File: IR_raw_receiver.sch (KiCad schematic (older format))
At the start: 5 parts

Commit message: Might be done already :-)
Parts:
- added C1: 47µF, symbol CP1
- added MH1, MH2, MH3, MH4: CONN_1, symbol CONN_1
- added P1: CONN_5, symbol CONN_5
- added R2, R3, R4, R5: 1k, symbol R
- JP1: renamed from JP?; value MADW__AVR_ISP -> ISP
- Q1: renamed from Q?; value CSTLA_T -> 8MHz
- R1: renamed from R?; value R -> 10k
- U1: renamed from U?; value MADW__TSOP38238 -> TSOP38238
- gave numbers to parts that had none: 1
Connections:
- net labels added: GND, MISO, MOSI, RESET, SCK, VCC, XTAL1, XTAL2
- wire segments 0 -> 38
- no-connect marks 0 -> 4
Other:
- moved on the sheet: IC1, JP1, Q1, R1, U1

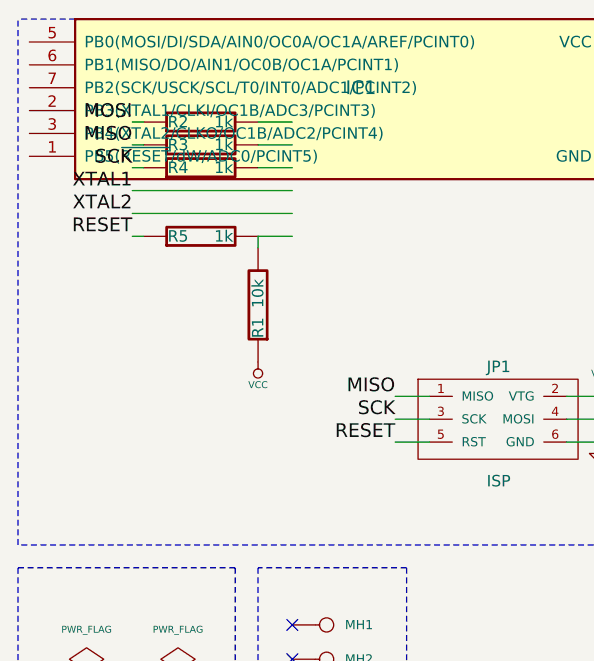
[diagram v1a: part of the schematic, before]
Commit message: Added a LED + some minor tweaks.
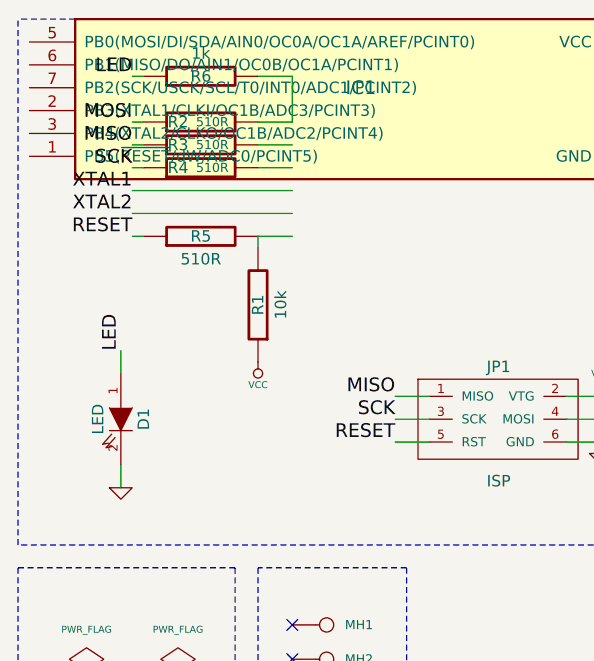
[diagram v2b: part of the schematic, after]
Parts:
- added D1: LED, symbol LED
- added R6: 1k, symbol R
- R2, R3, R4, R5: value 1k -> 510R
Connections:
- net labels added: LED
- wire segments 38 -> 43
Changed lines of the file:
@@
-EESchema Schematic File Version 2  date Sun 25 Mar 2012 02:18:25 PM CEST
+EESchema Schematic File Version 2  date Sun 25 Mar 2012 06:06:28 PM CEST
 LIBS:power
 LIBS:device
@@
 Comment4 ""
 $EndDescr
+Text Label 1650 2700 1    60   ~ 0
+LED
+Wire Wire Line
+	1650 2800 1650 2700
+Wire Wire Line
+	1750 1500 1700 1500
+Wire Notes Line
+	2900 3650 2250 3650
+Wire Notes Line
+	2900 3650 2900 4600
+Wire Notes Line
+	2900 4600 2250 4600
+Wire Notes Line
+	2250 4600 2250 3650
+Wire Notes Line
+	5650 1250 1200 1250
+Wire Notes Line
+	5650 1250 5650 3550
+Wire Notes Line
+	5650 3550 1200 3550
+Wire Notes Line
+	1200 3550 1200 1250
+Connection ~ 5200 2200
+Wire Wire Line
+	5200 2150 5200 2250
+Wire Wire Line
+	6850 1900 6950 1900
+Wire Wire Line
+	1700 1700 1750 1700
+Wire Wire Line
+	1700 1900 1750 1900
+Wire Wire Line
+	1700 2100 2400 2100
+Wire Wire Line
+	6250 3150 6350 3150
+Wire Wire Line
+	1900 4150 1900 4250
+Wire Wire Line
+	6950 2300 6950 2250
+Wire Wire Line
+	6950 2250 6850 2250
+Wire Wire Line
+	5200 2200 5100 2200
+Wire Wire Line
+	2250 1700 2400 1700
+Wire Wire Line
+	2250 1900 2400 1900
+Wire Wire Line
+	4800 2900 4850 2900
+Wire Wire Line
+	4600 3200 4600 3300
+Wire Wire Line
+	3600 3000 3750 3000
+Wire Wire Line
+	3000 3100 2850 3100
+Wire Wire Line
+	3000 2900 2850 2900
+Wire Wire Line
+	2250 2250 2250 2200
+Wire Wire Line
+	2250 2200 2400 2200
+Wire Wire Line
+	3000 3000 2850 3000
+Wire Wire Line
+	3600 2900 3750 2900
+Wire Wire Line
+	3600 3100 3750 3100
+Wire Wire Line
+	4400 2900 4350 2900
+Wire Wire Line
+	3750 3100 3750 3150
+Wire Wire Line
+	2250 1800 2400 1800
+Wire Wire Line
+	5100 1700 5200 1700
+Wire Wire Line
+	6850 1550 6950 1550
+Wire Wire Line
+	6950 1550 6950 1500
+Wire Wire Line
+	1500 4150 1500 4250
+Wire Wire Line
+	6350 2850 6250 2850
+Wire Wire Line
+	6250 3050 6350 3050
+Wire Wire Line
+	6350 3250 6250 3250
+Wire Wire Line
+	2400 2000 1700 2000
+Wire Wire Line
+	1750 1800 1700 1800
+Wire Wire Line
+	1700 2200 1750 2200
+Wire Wire Line
+	6150 2900 6150 2950
+Wire Wire Line
+	6150 2950 6350 2950
+Wire Wire Line
+	5200 1700 5200 1750
+Wire Notes Line
+	1200 4600 1200 3650
+Wire Notes Line
+	1200 4600 2150 4600
+Wire Notes Line
+	1200 3650 2150 3650
+Wire Notes Line
+	5800 3550 5800 1250
+Wire Notes Line
+	5800 3550 7350 3550
+Wire Notes Line
+	7350 3550 7350 1250
+Wire Notes Line
+	7350 1250 5800 1250
+Wire Notes Line
+	2150 3650 2150 4600
+Wire Wire Line
+	2250 1500 2400 1500
+Wire Wire Line
+	2400 1500 2400 1700
+Wire Wire Line
+	1650 3200 1650 3300
+$Comp
+L GND #PWR01
+U 1 1 4F6F3657
+P 1650 3300
+F 0 "#PWR01" H 1650 3300 30  0001 C CNN
+F 1 "GND" H 1650 3230 30  0001 C CNN
+	1    1650 3300
+	1    0    0    -1
+$EndComp
+Text Label 1700 1500 2    60   ~ 0
+LED
+$Comp
+L LED D1
+U 1 1 4F6F3628
+P 1650 3000
+F 0 "D1" H 1650 3100 50  0000 C CNN
+F 1 "LED" H 1650 2900 50  0000 C CNN
+	1    1650 3000
+	0    1    1    0
+$EndComp
+$Comp
+L R R6
+U 1 1 4F6F35F5
+P 2000 1500
+F 0 "R6" V 2000 1500 50  0000 C CNN
+F 1 "1k" V 2100 1500 50  0000 C CNN
+	1    2000 1500
+	0    -1   -1   0
+$EndComp
 NoConn ~ 2400 4350
 NoConn ~ 2400 4200
 NoConn ~ 2400 4050
 NoConn ~ 2400 3900
-Wire Notes Line
-	2900 3650 2250 3650
-Wire Notes Line
-	2900 3650 2900 4600
-Wire Notes Line
-	2900 4600 2250 4600
-Wire Notes Line
-	2250 4600 2250 3650
-Wire Notes Line
-	5650 1250 1200 1250
-Wire Notes Line
-	5650 1250 5650 3550
-Wire Notes Line
-	5650 3550 1200 3550
-Wire Notes Line
-	1200 3550 1200 1250
-Connection ~ 5200 2200
-Wire Wire Line
-	5200 2150 5200 2250
-Wire Wire Line
-	6850 1900 6950 1900
-Wire Wire Line
-	1700 1700 1750 1700
-Wire Wire Line
-	1700 1900 1750 1900
-Wire Wire Line
-	1700 2100 2400 2100
-Wire Wire Line
-	6250 3150 6350 3150
-Wire Wire Line
-	1900 4150 1900 4250
-Wire Wire Line
-	6950 2300 6950 2250
-Wire Wire Line
-	6950 2250 6850 2250
-Wire Wire Line
-	5200 2200 5100 2200
-Wire Wire Line
-	2250 1700 2400 1700
-Wire Wire Line
-	2250 1900 2400 1900
-Wire Wire Line
-	4800 2900 4850 2900
-Wire Wire Line
-	4600 3200 4600 3300
-Wire Wire Line
-	3600 3000 3750 3000
-Wire Wire Line
-	3000 3100 2850 3100
-Wire Wire Line
-	3000 2900 2850 2900
-Wire Wire Line
-	2250 2250 2250 2200
-Wire Wire Line
-	2250 2200 2400 2200
-Wire Wire Line
-	3000 3000 2850 3000
-Wire Wire Line
-	3600 2900 3750 2900
-Wire Wire Line
-	3600 3100 3750 3100
-Wire Wire Line
-	4400 2900 4350 2900
-Wire Wire Line
-	3750 3100 3750 3150
-Wire Wire Line
-	2250 1800 2400 1800
-Wire Wire Line
-	5100 1700 5200 1700
-Wire Wire Line
-	6850 1550 6950 1550
-Wire Wire Line
-	6950 1550 6950 1500
-Wire Wire Line
-	1500 4150 1500 4250
-Wire Wire Line
-	6350 2850 6250 2850
-Wire Wire Line
-	6250 3050 6350 3050
-Wire Wire Line
-	6350 3250 6250 3250
-Wire Wire Line
-	2400 2000 1700 2000
-Wire Wire Line
-	1750 1800 1700 1800
-Wire Wire Line
-	1700 2200 1750 2200
-Wire Wire Line
-	6150 2900 6150 2950
-Wire Wire Line
-	6150 2950 6350 2950
-Wire Wire Line
-	5200 1700 5200 1750
-Wire Notes Line
-	1200 4600 1200 3650
-Wire Notes Line
-	1200 4600 2150 4600
-Wire Notes Line
-	1200 3650 2150 3650
-Wire Notes Line
-	5800 3550 5800 1250
-Wire Notes Line
-	5800 3550 7350 3550
-Wire Notes Line
-	7350 3550 7350 1250
-Wire Notes Line
-	7350 1250 5800 1250
-Wire Notes Line
-	2150 3650 2150 4600
 $Comp
 L CONN_1 MH4
@@
 U 1 1 4F6EEBE3
 P 2000 2200
-F 0 "R5" V 2000 2300 50  0000 C CNN
-F 1 "1k" V 2000 2100 50  0000 C CNN
+F 0 "R5" V 2000 2200 50  0000 C CNN
+F 1 "510R" V 1900 2200 50  0000 C CNN
 	1    2000 2200
 	0    -1   -1   0
@@
 P 2000 1900
 F 0 "R4" V 2000 2000 50  0000 C CNN
-F 1 "1k" V 2000 1800 50  0000 C CNN
+F 1 "510R" V 2000 1850 40  0000 C CNN
 	1    2000 1900
 	0    -1   -1   0
@@
 P 2000 1800
 F 0 "R3" V 2000 1900 50  0000 C CNN
-F 1 "1k" V 2000 1700 50  0000 C CNN
+F 1 "510R" V 2000 1750 40  0000 C CNN
 	1    2000 1800
 	0    -1   -1   0
@@
 P 2000 1700
 F 0 "R2" V 2000 1800 50  0000 C CNN
-F 1 "1k" V 2000 1600 50  0000 C CNN
+F 1 "510R" V 2000 1650 40  0000 C CNN
 	1    2000 1700
 	0    -1   -1   0
@@
 MOSI
 $Comp
-L GND #PWR01
+L GND #PWR02
 U 1 1 4F6EEB7B
 P 6150 2900
-F 0 "#PWR01" H 6150 2900 30  0001 C CNN
+F 0 "#PWR02" H 6150 2900 30  0001 C CNN
 F 1 "GND" H 6150 2830 30  0001 C CNN
 	1    6150 2900
@@
 $EndComp
 $Comp
-L VCC #PWR02
+L VCC #PWR03
 U 1 1 4F6EEB71
 P 6250 2850
-F 0 "#PWR02" H 6250 2950 30  0001 C CNN
+F 0 "#PWR03" H 6250 2950 30  0001 C CNN
 F 1 "VCC" H 6250 2950 30  0000 C CNN
 	1    6250 2850
@@
 $EndComp
 $Comp
-L PWR_FLAG #FLG03
+L PWR_FLAG #FLG04
 U 1 1 4F6EE978
 P 1900 4150
-F 0 "#FLG03" H 1900 4420 30  0001 C CNN
+F 0 "#FLG04" H 1900 4420 30  0001 C CNN
 F 1 "PWR_FLAG" H 1900 4380 30  0000 C CNN
 	1    1900 4150
@@
 $EndComp
 $Comp
-L VCC #PWR04
+L VCC #PWR05
 U 1 1 4F6EE956
 P 1900 4250
-F 0 "#PWR04" H 1900 4350 30  0001 C CNN
+F 0 "#PWR05" H 1900 4350 30  0001 C CNN
 F 1 "VCC" H 1900 4350 30  0000 C CNN
 	1    1900 4250
@@
 $EndComp
 $Comp
-L GND #PWR05
+L GND #PWR06
 U 1 1 4F6EE953
 P 1500 4250
-F 0 "#PWR05" H 1500 4250 30  0001 C CNN
+F 0 "#PWR06" H 1500 4250 30  0001 C CNN
 F 1 "GND" H 1500 4180 30  0001 C CNN
 	1    1500 4250
@@
 RESET
 $Comp
-L PWR_FLAG #FLG06
+L PWR_FLAG #FLG07
 U 1 1 4F6EE916
 P 1500 4150
-F 0 "#FLG06" H 1500 4420 30  0001 C CNN
+F 0 "#FLG07" H 1500 4420 30  0001 C CNN
 F 1 "PWR_FLAG" H 1500 4380 30  0000 C CNN
 	1    1500 4150
@@
 $EndComp
 $Comp
-L GND #PWR07
+L GND #PWR08
 U 1 1 4F6EE8F0
 P 6950 2300
-F 0 "#PWR07" H 6950 2300 30  0001 C CNN
+F 0 "#PWR08" H 6950 2300 30  0001 C CNN
 F 1 "GND" H 6950 2230 30  0001 C CNN
 	1    6950 2300
@@
 $EndComp
 $Comp
-L VCC #PWR08
+L VCC #PWR09
 U 1 1 4F6EE8E3
 P 6950 1500
-F 0 "#PWR08" H 6950 1600 30  0001 C CNN
+F 0 "#PWR09" H 6950 1600 30  0001 C CNN
 F 1 "VCC" H 6950 1600 30  0000 C CNN
 	1    6950 1500
@@
 $EndComp
 $Comp
-L VCC #PWR09
+L VCC #PWR010
 U 1 1 4F6EE887
 P 5200 1700
-F 0 "#PWR09" H 5200 1800 30  0001 C CNN
+F 0 "#PWR010" H 5200 1800 30  0001 C CNN
 F 1 "VCC" H 5200 1800 30  0000 C CNN
 	1    5200 1700
@@
 $EndComp
 $Comp
-L GND #PWR010
+L GND #PWR011
 U 1 1 4F6EE882
 P 5200 2250
-F 0 "#PWR010" H 5200 2250 30  0001 C CNN
+F 0 "#PWR011" H 5200 2250 30  0001 C CNN
 F 1 "GND" H 5200 2180 30  0001 C CNN
 	1    5200 2250
@@
 MOSI
 $Comp
-L GND #PWR011
+L GND #PWR012
 U 1 1 4F6EE81E
 P 3750 3150
-F 0 "#PWR011" H 3750 3150 30  0001 C CNN
+F 0 "#PWR012" H 3750 3150 30  0001 C CNN
 F 1 "GND" H 3750 3080 30  0001 C CNN
 	1    3750 3150
@@
 MOSI
 $Comp
-L VCC #PWR012
+L VCC #PWR013
 U 1 1 4F6EE80A
 P 3750 2900
-F 0 "#PWR012" H 3750 3000 30  0001 C CNN
+F 0 "#PWR013" H 3750 3000 30  0001 C CNN
 F 1 "VCC" H 3750 3000 30  0000 C CNN
 	1    3750 2900
@@
 XTAL2
 $Comp
-L GND #PWR013
+L GND #PWR014
 U 1 1 4F6EE7AB
 P 4600 3300
-F 0 "#PWR013" H 4600 3300 30  0001 C CNN
+F 0 "#PWR014" H 4600 3300 30  0001 C CNN
 F 1 "GND" H 4600 3230 30  0001 C CNN
 	1    4600 3300
@@
 $EndComp
 $Comp
-L VCC #PWR014
+L VCC #PWR015
 U 1 1 4F6EE70F
 P 2250 2750
-F 0 "#PWR014" H 2250 2850 30  0001 C CNN
+F 0 "#PWR015" H 2250 2850 30  0001 C CNN
 F 1 "VCC" H 2250 2850 30  0000 C CNN
 	1    2250 2750
@@
 U 1 1 4F6EC6DD
 P 2250 2500
-F 0 "R1" V 2250 2600 50  0000 C CNN
-F 1 "10k" V 2250 2450 50  0000 C CNN
+F 0 "R1" V 2250 2500 50  0000 C CNN
+F 1 "10k" V 2150 2500 50  0000 C CNN
 	1    2250 2500
 	-1   0    0    1

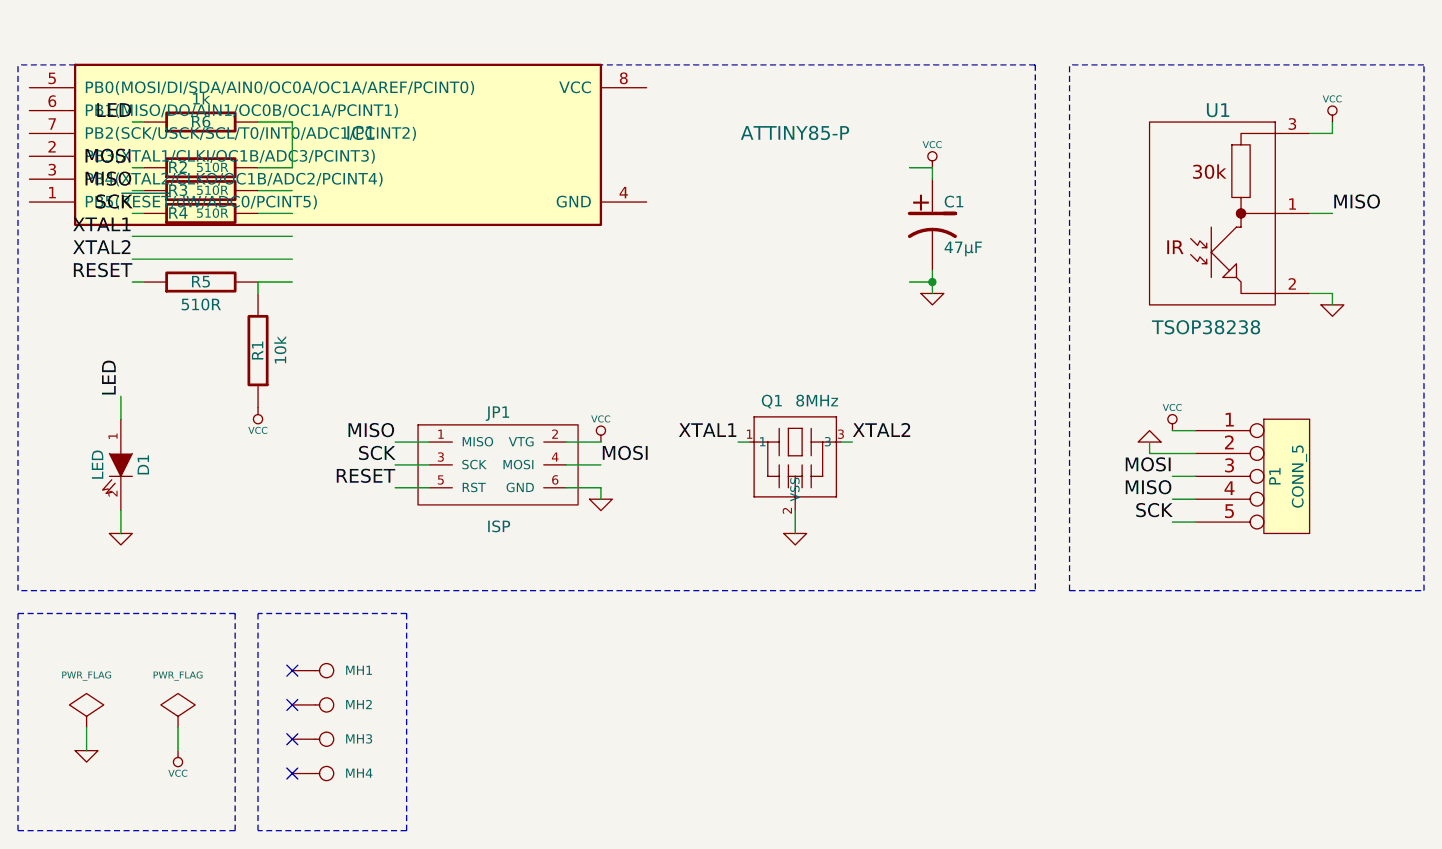
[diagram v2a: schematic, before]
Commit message: Added an L78L05 voltage regulator + caps. Header + silkscreen tweaks.
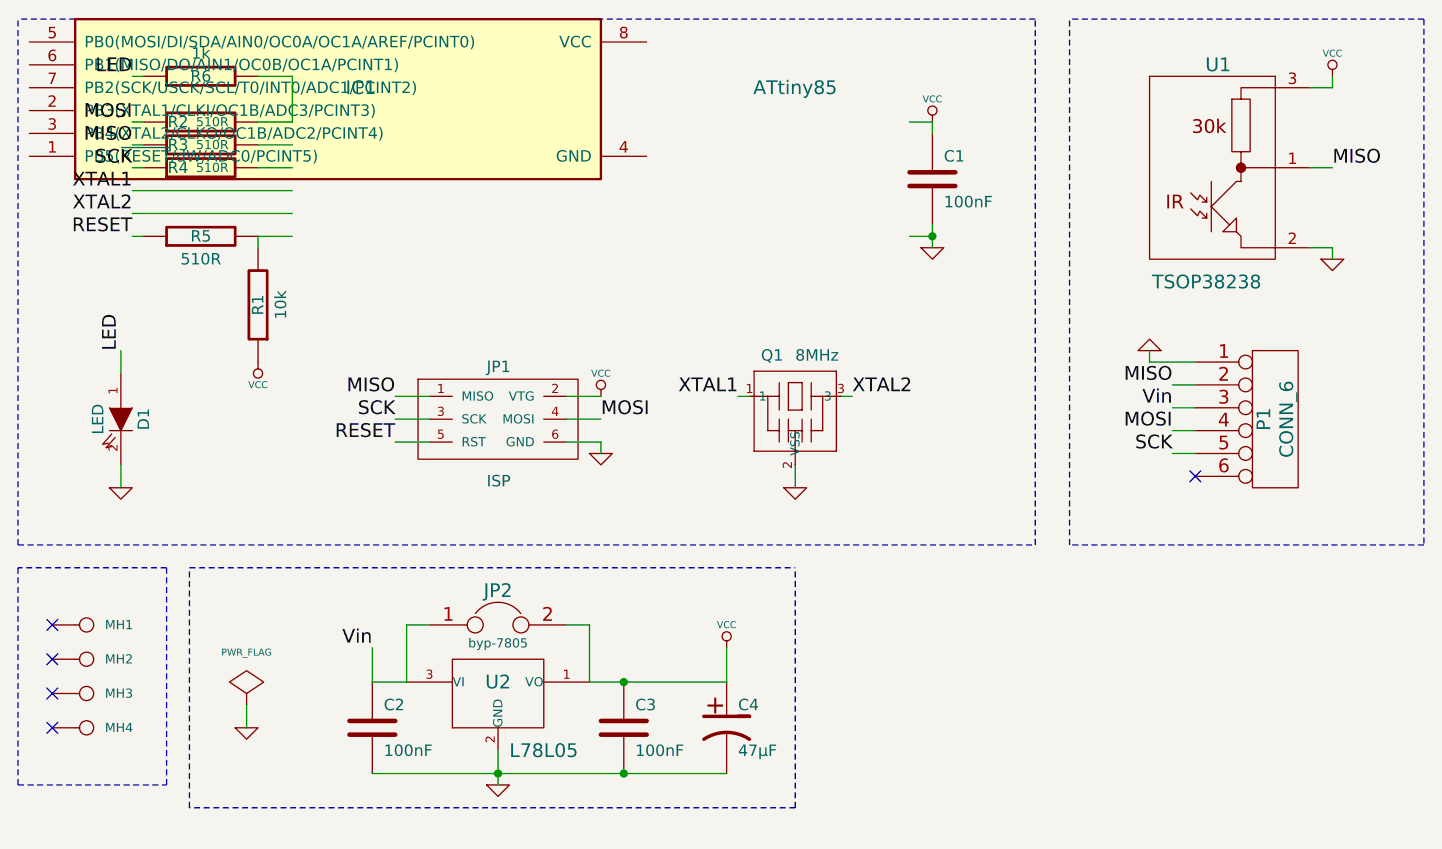
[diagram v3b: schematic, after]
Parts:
- removed P1: CONN_5, symbol CONN_5
- added C1, C2, C3: 100nF, symbol C
- added JP2: byp-7805, symbol JUMPER
- added P1: CONN_6, symbol CONN_6
- added U2: L78L05, symbol MADW__L78L05_TO-92
- IC1: value ATTINY85-P -> ATtiny85
- renumbered C1 to C4
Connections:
- net labels added: Vin
- wire segments 43 -> 52
- no-connect marks 4 -> 5
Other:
- moved on the sheet: C4, D1, IC1, JP1, MH1, MH2, MH3, MH4, Q1, R1, R2, R3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

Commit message: Silkscreen tweaks.
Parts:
- JP2: value byp-7805 -> Vin!
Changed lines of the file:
@@
-EESchema Schematic File Version 2  date Sat 31 Mar 2012 04:20:52 PM CEST
+EESchema Schematic File Version 2  date Sat 31 Mar 2012 09:51:07 PM CEST
 LIBS:power
 LIBS:device
@@
 P 3300 3700
 F 0 "JP2" H 3300 3850 60  0000 C CNN
-F 1 "byp-7805" H 3300 3620 40  0000 C CNN
+F 1 "Vin!" H 3300 3620 40  0000 C CNN
 	1    3300 3700
 	1    0    0    -1

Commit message: Switched to REV. 202 of atmel.lib
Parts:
- IC1: value ATtiny85 -> ATTINY85-P
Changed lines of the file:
@@
-EESchema Schematic File Version 2  date Sat 31 Mar 2012 09:51:07 PM CEST
+EESchema Schematic File Version 2  date Sun 27 Jan 2013 10:27:36 AM CET
 LIBS:power
 LIBS:device
@@
 LIBS:contrib
 LIBS:valves
-LIBS:atmel_rev110
 LIBS:my_parts
 LIBS:murata-resonators
 LIBS:IR_raw_receiver-cache
-EELAYER 25  0
+EELAYER 27 0
 EELAYER END
 $Descr User 8267 5905
@@
 Sheet 1 1
 Title "IR_raw_receiver"
-Date "31 mar 2012"
+Date "27 jan 2013"
 Rev "1.10"
 Comp "2012 - blog.spitzenpfeil.org"
@@
 $Comp
 L ATTINY85-P IC1
-U 1 1 4F6EC673
-P 2600 1400
-F 0 "IC1" H 2700 1450 60  0000 C CNN
-F 1 "ATtiny85" H 4600 1450 60  0000 C CNN
-F 2 "DIP8" H 2700 650 60  0001 C CNN
-	1    2600 1400
-	1    0    0    -1
-$EndComp
+U 1 1 5104F2A5
+P 3750 1750
+F 0 "IC1" H 2700 2150 60  0000 C CNN
+F 1 "ATTINY85-P" H 4600 1350 60  0000 C CNN
+F 2 "DIP8" H 2700 1350 60  0001 C CNN
+	1    3750 1750
+	1    0    0    -1
+$EndComp
